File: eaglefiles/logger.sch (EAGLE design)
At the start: 35 parts, among them K1 65100516121, Q2 IRLML9301, U1 MCP1640, U3 FT232RLSSOP

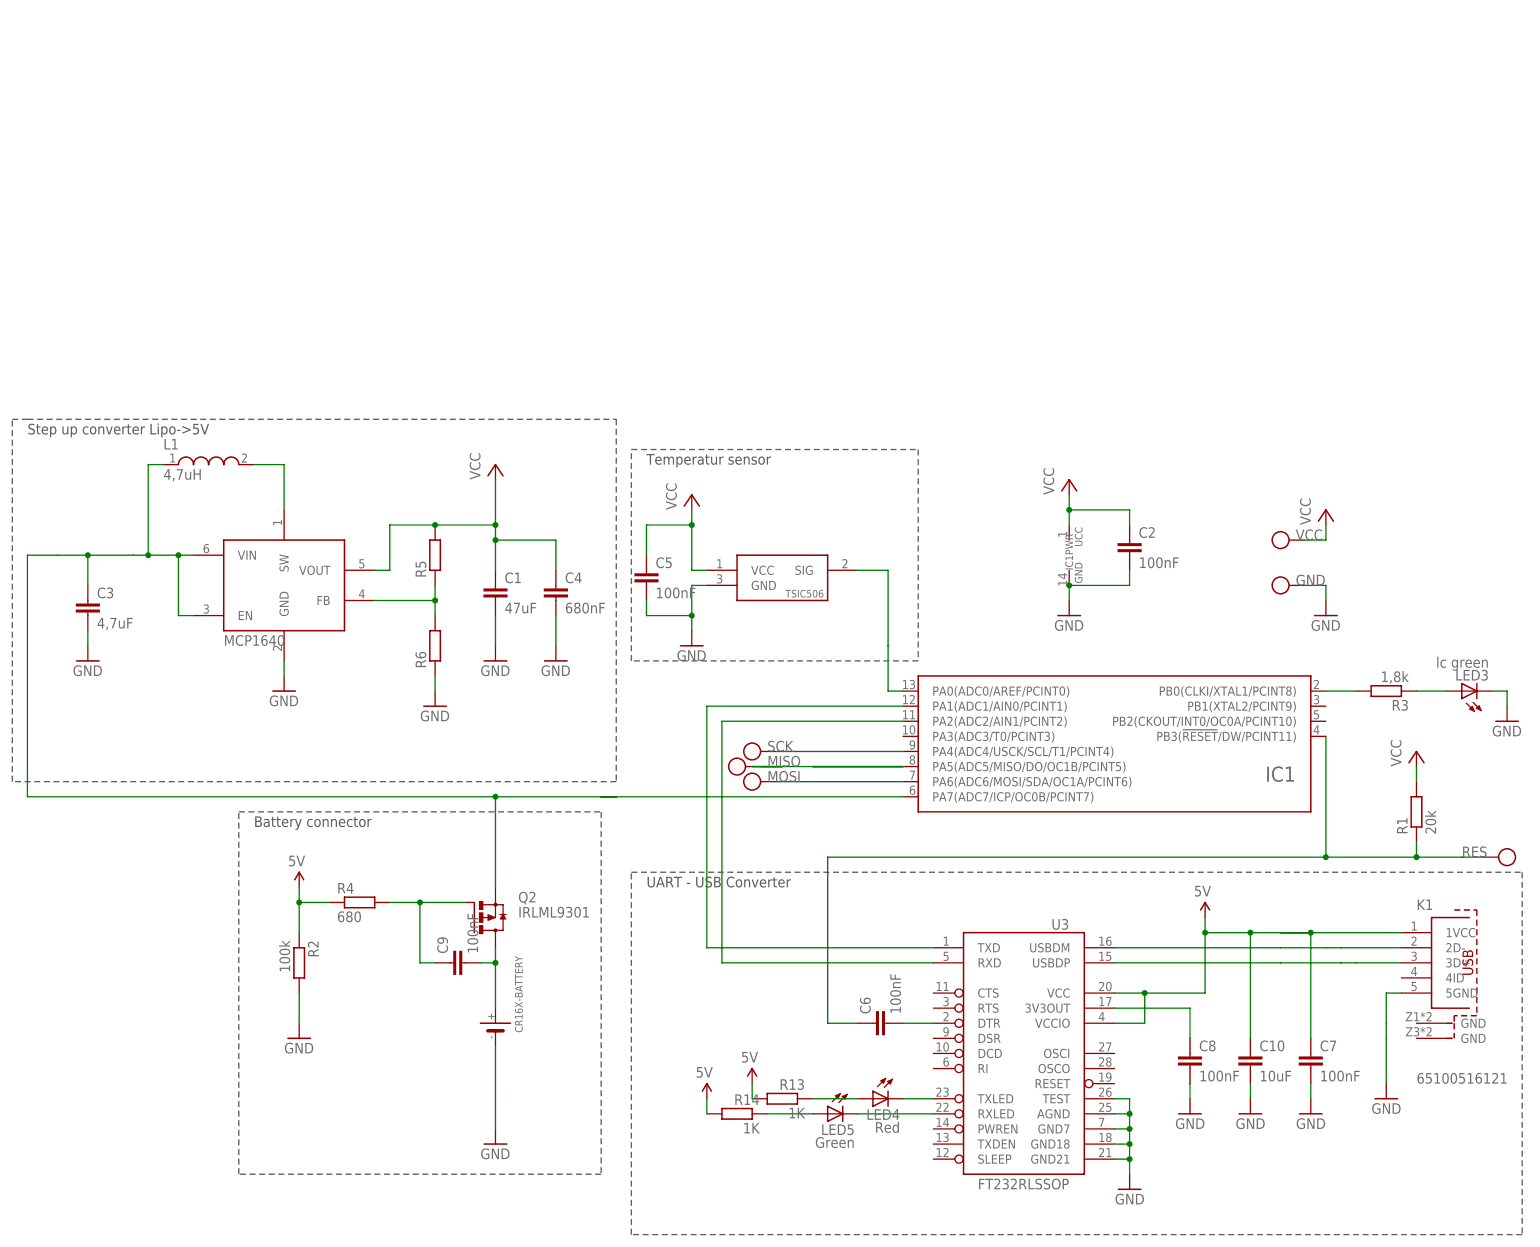
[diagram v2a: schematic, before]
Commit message: Corrected direction of mosfet & copied lib for tsic
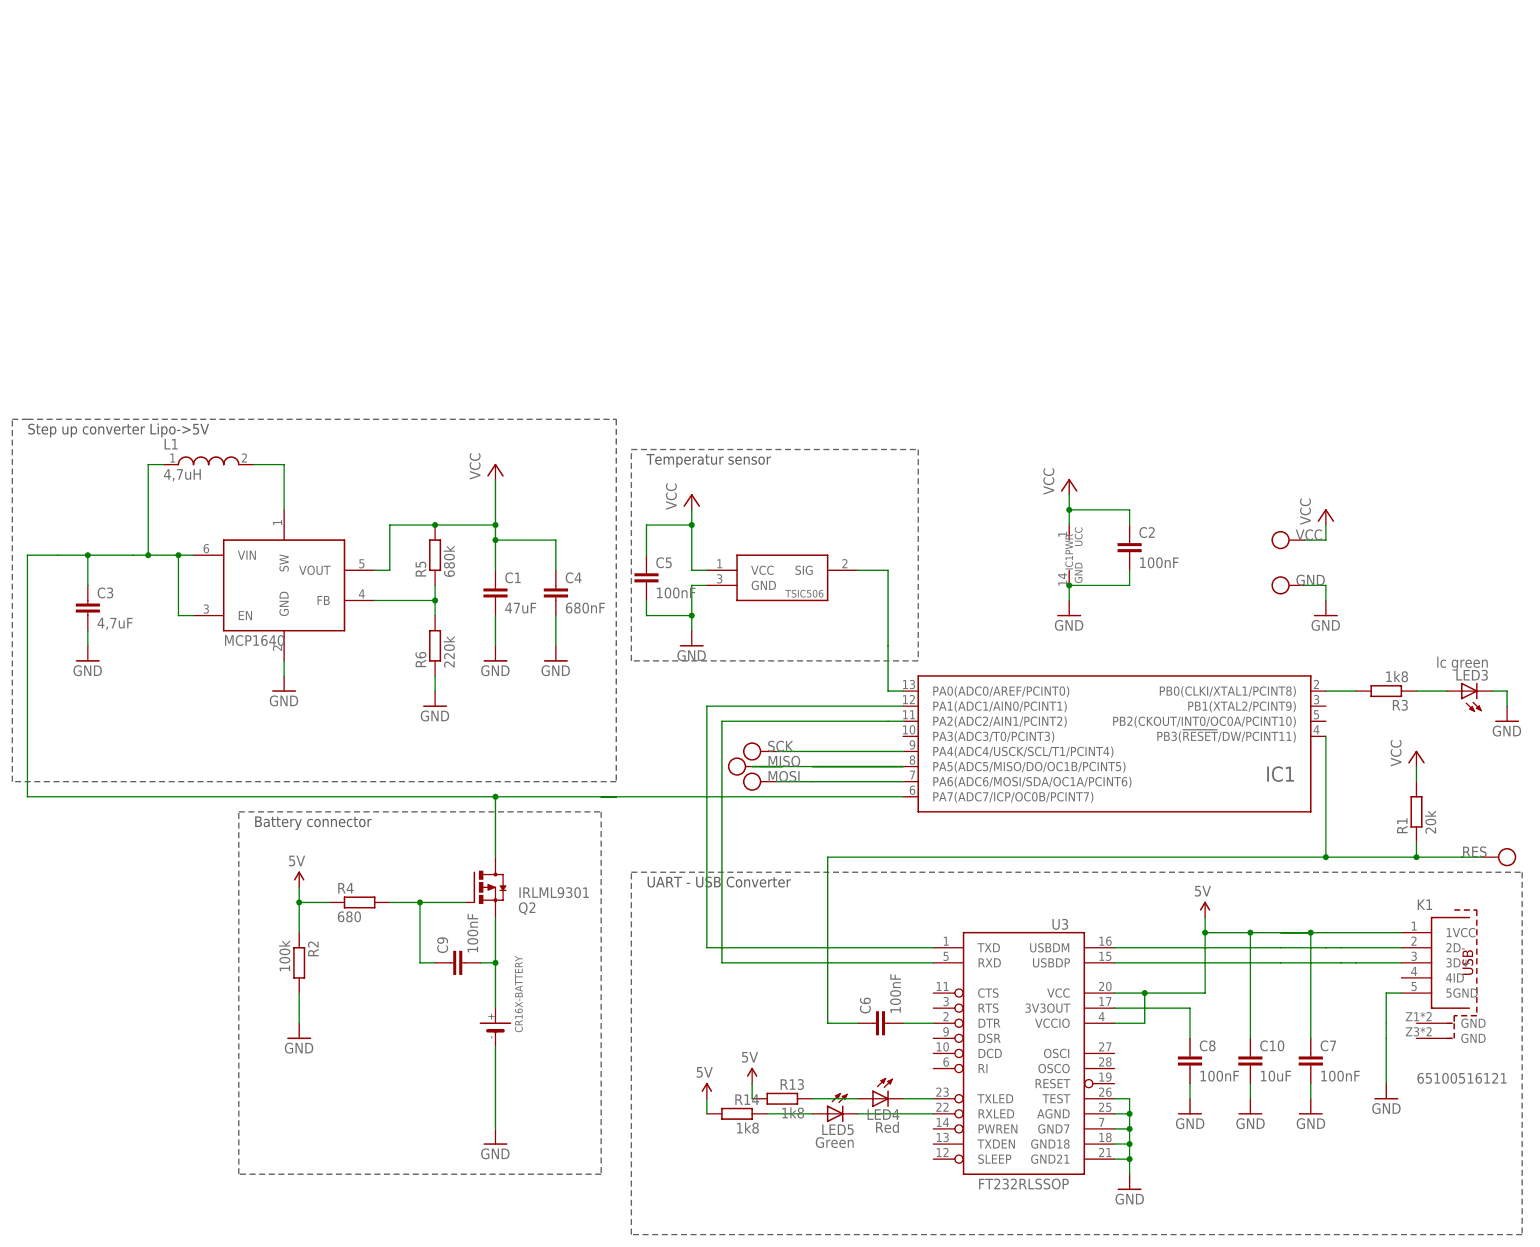
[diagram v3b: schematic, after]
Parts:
- R13, R14: value 1K -> 1k8
- R3: value 1,8k -> 1k8
- R5: value (none) -> 680k
- R6: value (none) -> 220k
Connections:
- net N$6: now also Q2.S; no longer Q2.D
- net VSUPPLY: now also Q2.D; no longer Q2.S
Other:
- moved on the sheet: Q2
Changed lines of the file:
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@@
 <part name="VCC" library="supply1" deviceset="VCC" device=""/>
 <part name="LED3" library="led" deviceset="LED" device="CHIPLED_0603" value="lc green"/>
-<part name="R3" library="eagle-ltspice" deviceset="R" device="R1206" value="1,8k"/>
+<part name="R3" library="eagle-ltspice" deviceset="R" device="R1206" value="1k8"/>
 <part name="GND3" library="supply1" deviceset="GND" device=""/>
 <part name="GND11" library="supply1" deviceset="GND" device=""/>
@@
 <part name="C3" library="rcl" deviceset="C-EU" device="C1206K" value="4,7uF"/>
 <part name="GND8" library="supply1" deviceset="GND" device=""/>
-<part name="R5" library="resistor" deviceset="R-EU_" device="R1206"/>
-<part name="R6" library="resistor" deviceset="R-EU_" device="R1206"/>
+<part name="R5" library="resistor" deviceset="R-EU_" device="R1206" value="680k"/>
+<part name="R6" library="resistor" deviceset="R-EU_" device="R1206" value="220k"/>
 <part name="GND12" library="supply1" deviceset="GND" device=""/>
 <part name="L1" library="EagleLibrary_Wuerth_Elektronik_eiSos_rev16a" deviceset="WE-TPC" device="_3816" value="4,7uH"/>
@@
 <part name="GND14" library="SparkFun" deviceset="GND" device=""/>
 <part name="GND15" library="SparkFun" deviceset="GND" device=""/>
-<part name="R13" library="rcl" deviceset="R-EU_" device="R1206" value="1K"/>
-<part name="R14" library="rcl" deviceset="R-EU_" device="R1206" value="1K"/>
+<part name="R13" library="rcl" deviceset="R-EU_" device="R1206" value="1k8"/>
+<part name="R14" library="rcl" deviceset="R-EU_" device="R1206" value="1k8"/>
 <part name="LED4" library="SparkFun" deviceset="LED" device="0603" value="Red"/>
 <part name="LED5" library="SparkFun" deviceset="LED" device="0603" value="Green"/>
@@
 <instance part="U$3" gate="G$1" x="22.86" y="-40.64" rot="MR0"/>
 <instance part="U$4" gate="G$1" x="15.24" y="-43.18" rot="MR0"/>
-<instance part="Q2" gate="G$1" x="-22.86" y="-12.7"/>
+<instance part="Q2" gate="G$1" x="-22.86" y="-7.62" rot="MR180"/>
 <instance part="R2" gate="G$1" x="-53.34" y="-20.32" rot="R270"/>
 <instance part="GND1" gate="1" x="-53.34" y="-33.02"/>
@@
 <segment>
 <wire x1="0" y1="7.62" x2="-2.54" y2="7.62" width="0.1524" layer="91"/>
-<wire x1="-20.32" y1="-7.62" x2="-20.32" y2="-5.08" width="0.1524" layer="91"/>
-<wire x1="-20.32" y1="-5.08" x2="-20.32" y2="7.62" width="0.1524" layer="91"/>
+<wire x1="-20.32" y1="-2.54" x2="-20.32" y2="7.62" width="0.1524" layer="91"/>
 <wire x1="-20.32" y1="7.62" x2="-2.54" y2="7.62" width="0.1524" layer="91"/>
 <wire x1="-2.54" y1="7.62" x2="0" y2="7.62" width="0.1524" layer="91"/>
@@
 <pinref part="IC1" gate="IC" pin="PA7(ADC7/ICP/OC0B/PCINT7)"/>
 <wire x1="48.26" y1="7.62" x2="0" y2="7.62" width="0.1524" layer="91"/>
-<pinref part="Q2" gate="G$1" pin="S"/>
 <wire x1="-99.06" y1="48.26" x2="-99.06" y2="7.62" width="0.1524" layer="91"/>
 <wire x1="-99.06" y1="7.62" x2="-20.32" y2="7.62" width="0.1524" layer="91"/>
+<pinref part="Q2" gate="G$1" pin="D"/>
 </segment>
 </net>
@@
 <pinref part="U$1" gate="G$1" pin="P$1"/>
 <wire x1="-20.32" y1="-27.8892" x2="-20.32" y2="-20.32" width="0.1524" layer="91"/>
-<pinref part="Q2" gate="G$1" pin="D"/>
 <pinref part="C9" gate="G$1" pin="2"/>
-<wire x1="-20.32" y1="-20.32" x2="-20.32" y2="-17.78" width="0.1524" layer="91"/>
 <wire x1="-20.32" y1="-20.32" x2="-22.86" y2="-20.32" width="0.1524" layer="91"/>
+<pinref part="Q2" gate="G$1" pin="S"/>
+<wire x1="-20.32" y1="-12.7" x2="-20.32" y2="-20.32" width="0.1524" layer="91"/>
 <junction x="-20.32" y="-20.32"/>
 </segment>

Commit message: Added diode for 5V usb port
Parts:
- added D3: PMEG2010AET, diode:BAS70
- added R7: 220, resistor:R-EU_R1206
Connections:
- new net N$10: C5.1, R7.2, U$2.VCC
- new net N$9: IC1IC.PA3(ADC3/T0/PCINT3), R7.1
- net 5V: now also D3.A
- net VCC: now also D3.C; no longer C5.1, U$2.VCC
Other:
- moved on the sheet: R4

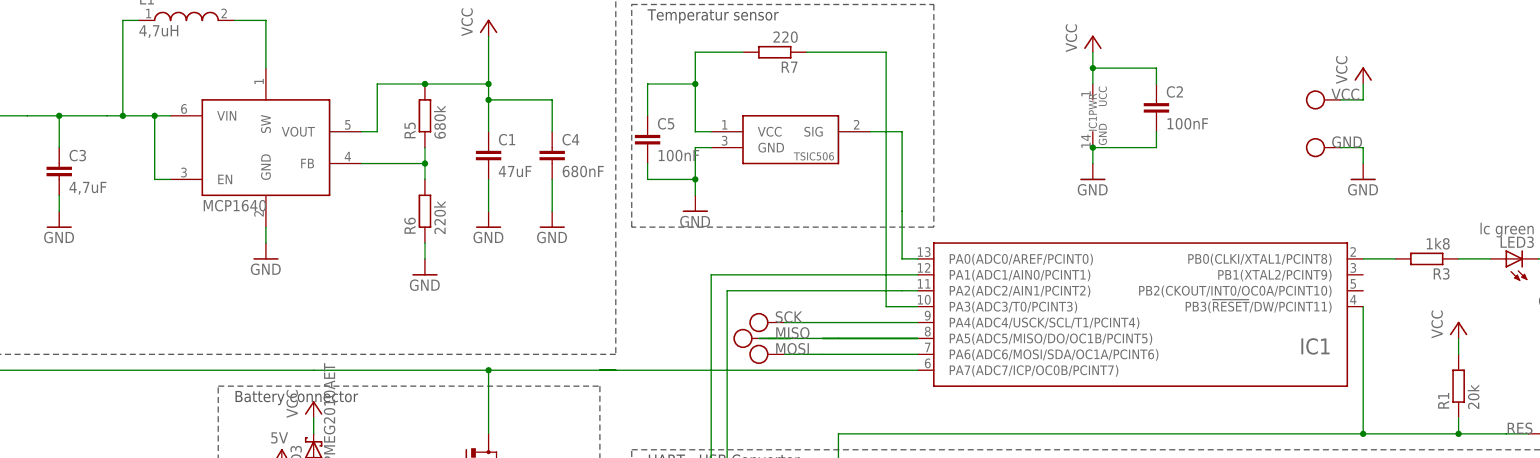
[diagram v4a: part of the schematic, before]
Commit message: Added option to trigger 5V supply voltage only on demand
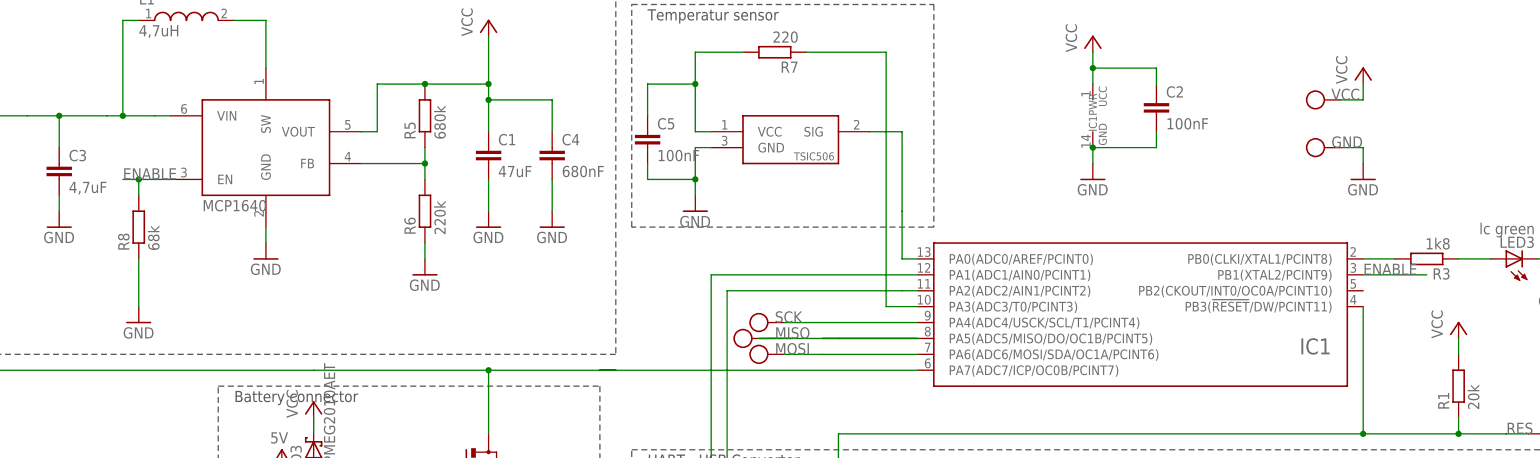
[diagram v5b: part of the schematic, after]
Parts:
- added R8: 68k, resistor:R-EU_R1206
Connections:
- new net ENABLE: IC1IC.PB1(XTAL2/PCINT9), R8.2, U1.EN
- net GND: now also R8.1
- net VSUPPLY: no longer U1.EN
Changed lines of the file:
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@@
 <part name="D3" library="diode" deviceset="BAS70" device="" value="PMEG2010AET"/>
 <part name="P+1" library="supply1" deviceset="VCC" device=""/>
+<part name="R8" library="resistor" deviceset="R-EU_" device="R1206" value="68k"/>
+<part name="GND13" library="supply1" deviceset="GND" device=""/>
 </parts>
 <sheets>
@@
 <instance part="D3" gate="1" x="-48.26" y="-5.08" rot="R90"/>
 <instance part="P+1" gate="VCC" x="-48.26" y="2.54"/>
+<instance part="R8" gate="G$1" x="-76.2" y="30.48" rot="R90"/>
+<instance part="GND13" gate="1" x="-76.2" y="15.24"/>
 </instances>
 <busses>
@@
 <wire x1="129.54" y1="-33.02" x2="129.54" y2="-40.64" width="0.1524" layer="91"/>
 </segment>
+<segment>
+<pinref part="R8" gate="G$1" pin="1"/>
+<pinref part="GND13" gate="1" pin="GND"/>
+<wire x1="-76.2" y1="25.4" x2="-76.2" y2="17.78" width="0.1524" layer="91"/>
+</segment>
 </net>
 <net name="VSUPPLY" class="0">
@@
 <wire x1="-78.74" y1="63.5" x2="-78.74" y2="48.26" width="0.1524" layer="91"/>
 <junction x="-78.74" y="48.26"/>
-<wire x1="-73.66" y1="48.26" x2="-73.66" y2="38.1" width="0.1524" layer="91"/>
-<junction x="-73.66" y="48.26"/>
-<wire x1="-73.66" y1="38.1" x2="-71.12" y2="38.1" width="0.1524" layer="91"/>
-<pinref part="U1" gate="G$1" pin="EN"/>
 <pinref part="C3" gate="G$1" pin="1"/>
 <wire x1="-88.9" y1="48.26" x2="-88.9" y2="43.18" width="0.1524" layer="91"/>
@@
 </segment>
 </net>
+<net name="ENABLE" class="0">
+<segment>
+<pinref part="IC1" gate="IC" pin="PB1(XTAL2/PCINT9)"/>
+<wire x1="119.38" y1="22.86" x2="129.54" y2="22.86" width="0.1524" layer="91"/>
+<label x="119.38" y="22.86" size="1.778" layer="95"/>
+</segment>
+<segment>
+<wire x1="-78.74" y1="38.1" x2="-76.2" y2="38.1" width="0.1524" layer="91"/>
+<pinref part="U1" gate="G$1" pin="EN"/>
+<label x="-78.74" y="38.1" size="1.778" layer="95"/>
+<pinref part="R8" gate="G$1" pin="2"/>
+<wire x1="-76.2" y1="38.1" x2="-71.12" y2="38.1" width="0.1524" layer="91"/>
+<wire x1="-76.2" y1="38.1" x2="-76.2" y2="35.56" width="0.1524" layer="91"/>
+<junction x="-76.2" y="38.1"/>
+</segment>
+</net>

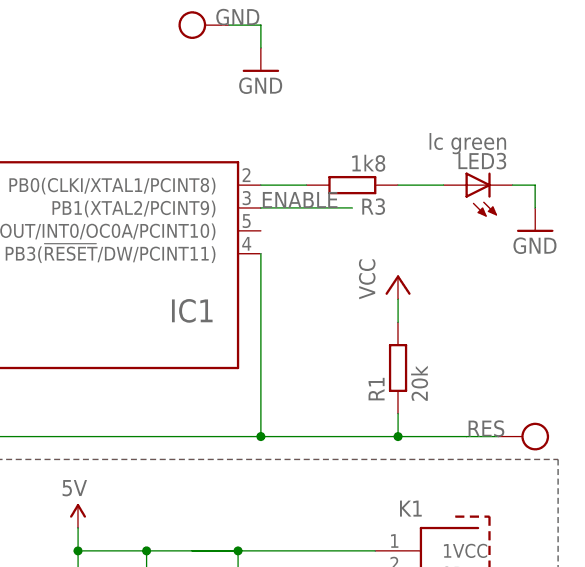
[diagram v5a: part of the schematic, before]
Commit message: Adjusted reverse voltage of uart -> FT232 VCC
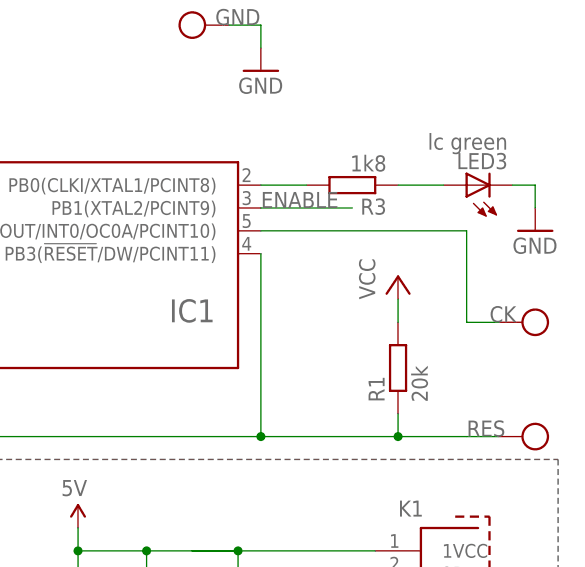
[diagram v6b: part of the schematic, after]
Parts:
- added U$13: (no value), 0liver:PIN1.27
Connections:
- new net CK: IC1IC.PB2(CKOUT/INT0/OC0A/PCINT10), U$13.P$1
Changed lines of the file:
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@@
 <part name="R8" library="resistor" deviceset="R-EU_" device="R1206" value="68k"/>
 <part name="GND13" library="supply1" deviceset="GND" device=""/>
+<part name="U$13" library="0liver" deviceset="PIN" device="1.27"/>
 </parts>
 <sheets>
@@
 <instance part="R8" gate="G$1" x="-76.2" y="30.48" rot="R90"/>
 <instance part="GND13" gate="1" x="-76.2" y="15.24"/>
+<instance part="U$13" gate="G$1" x="149.86" y="10.16" rot="R270"/>
 </instances>
 <busses>
@@
 </segment>
 </net>
+<net name="CK" class="0">
+<segment>
+<pinref part="IC1" gate="IC" pin="PB2(CKOUT/INT0/OC0A/PCINT10)"/>
+<wire x1="119.38" y1="20.32" x2="142.24" y2="20.32" width="0.1524" layer="91"/>
+<wire x1="142.24" y1="20.32" x2="142.24" y2="10.16" width="0.1524" layer="91"/>
+<pinref part="U$13" gate="G$1" pin="P$1"/>
+<wire x1="145.8" y1="10.16" x2="142.24" y2="10.16" width="0.1524" layer="91"/>
+<label x="144.78" y="10.16" size="1.778" layer="95"/>
+</segment>
+</net>
